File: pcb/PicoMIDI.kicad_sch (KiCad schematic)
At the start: 11 parts, among them J1 DIN-5, J2 DIN-5, J3 AudioJack3_SwitchTR, J4 AudioJack3_SwitchTR, U1 RP2040, U2 6N138

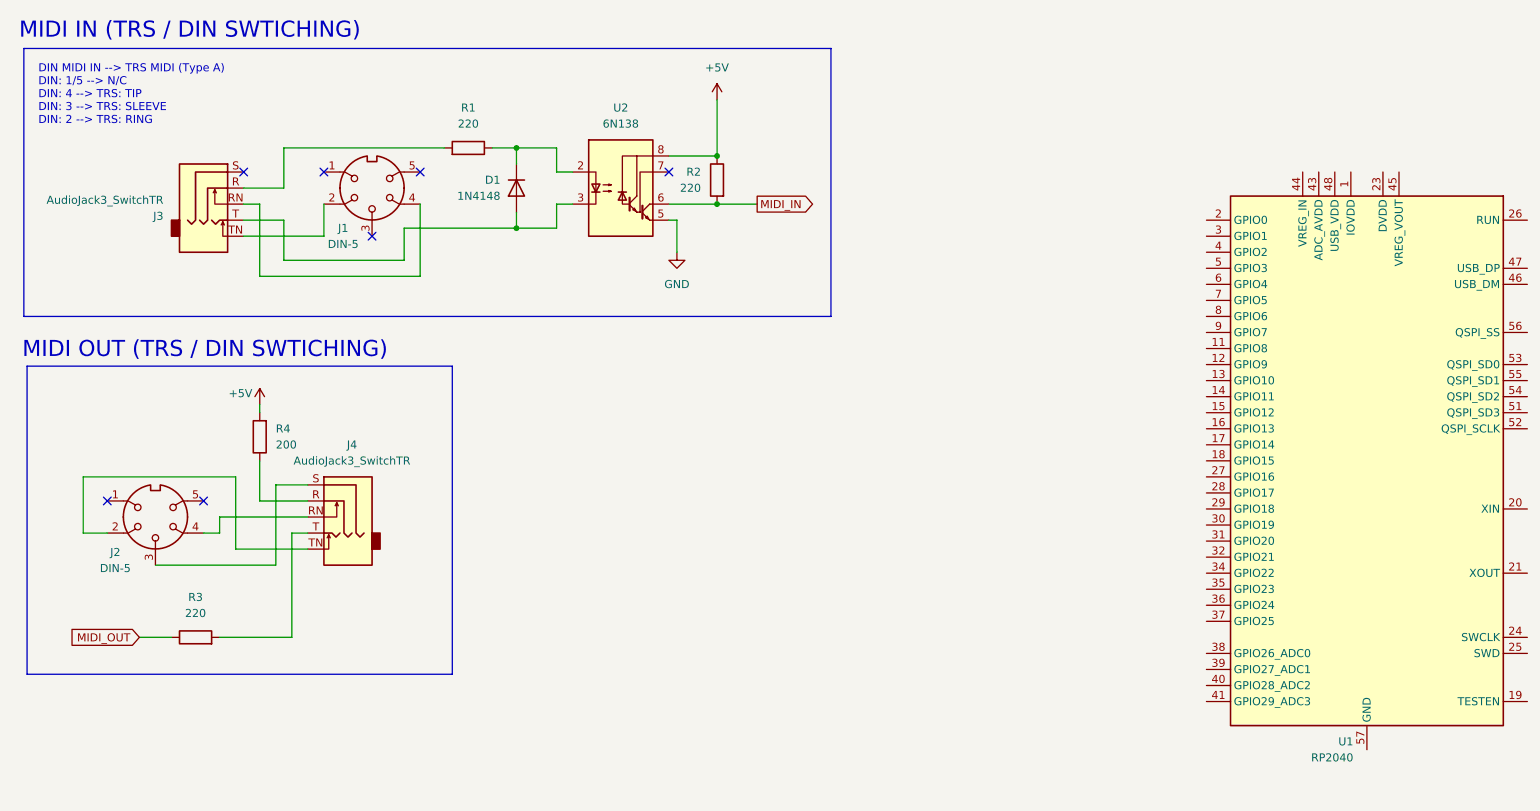
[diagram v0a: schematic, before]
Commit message: update schematic
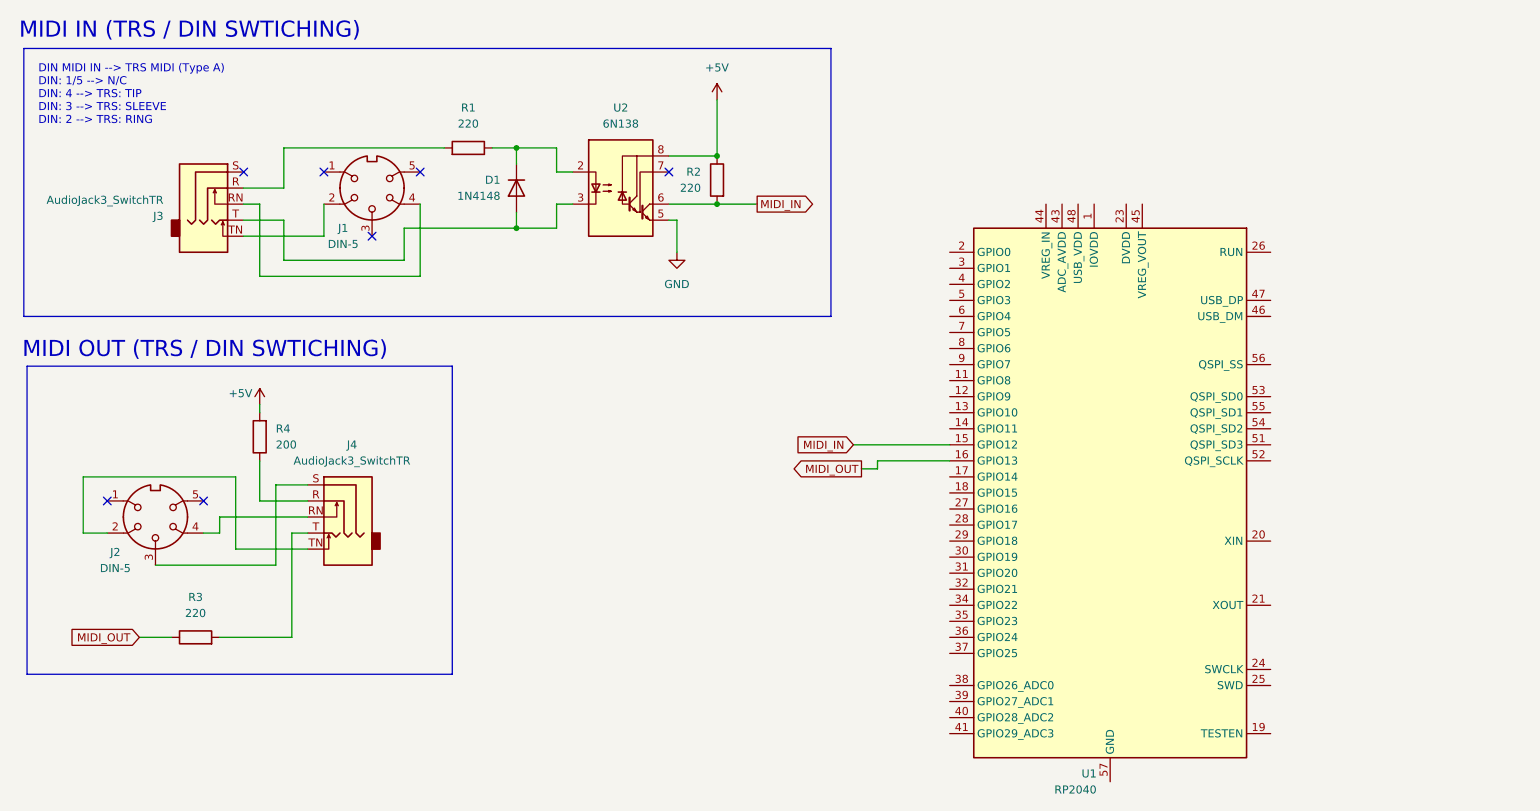
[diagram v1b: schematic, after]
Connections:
- net MIDI_IN: now also U1.15 (GPIO12)
- net MIDI_OUT: now also U1.16 (GPIO13)
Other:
- moved on the sheet: U1
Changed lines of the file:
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@@
+	(wire
+		(pts
+			(xy 149.86 86.36) (xy 161.29 86.36)
+		)
+		(stroke
+			(width 0)
+			(type default)
+		)
+	)
 	(wire
 		(pts
@@
 	(wire
 		(pts
+			(xy 146.05 83.82) (xy 161.29 83.82)
+		)
+		(stroke
+			(width 0)
+			(type default)
+		)
+	)
+	(wire
+		(pts
 			(xy 55.88 54.61) (xy 55.88 48.26)
 		)
@@
 	(wire
 		(pts
+			(xy 147.32 87.63) (xy 149.86 87.63)
+		)
+		(stroke
+			(width 0)
+			(type default)
+		)
+	)
+	(wire
+		(pts
 			(xy 54.61 90.17) (xy 59.69 90.17)
 		)
@@
 			(type default)
 			(color 132 0 132 1)
+		)
+	)
+	(wire
+		(pts
+			(xy 149.86 87.63) (xy 149.86 86.36)
+		)
+		(stroke
+			(width 0)
+			(type default)
 		)
 	)
@@
 	)
 	(global_label "MIDI_IN"
+		(shape input)
+		(at 146.05 83.82 180)
+		(fields_autoplaced yes)
+		(effects
+			(font
+				(size 1.27 1.27)
+			)
+			(justify right)
+		)
+		(property "Intersheetrefs" "${INTERSHEET_REFS}"
+			(at 136.2309 83.82 0)
+			(effects
+				(font
+					(size 1.27 1.27)
+				)
+				(justify right)
+				(hide yes)
+			)
+		)
+	)
+	(global_label "MIDI_IN"
 		(shape output)
 		(at 130.81 45.72 0)
@@
 				)
 				(justify left)
+				(hide yes)
+			)
+		)
+	)
+	(global_label "MIDI_OUT"
+		(shape output)
+		(at 147.32 87.63 180)
+		(fields_autoplaced yes)
+		(effects
+			(font
+				(size 1.27 1.27)
+			)
+			(justify right)
+		)
+		(property "Intersheetrefs" "${INTERSHEET_REFS}"
+			(at 135.8076 87.63 0)
+			(effects
+				(font
+					(size 1.27 1.27)
+				)
+				(justify right)
 				(hide yes)
 			)
@@
 	(symbol
 		(lib_id "MCU_RaspberryPi:RP2040")
-		(at 227.33 86.36 0)
+		(at 186.69 91.44 0)
 		(mirror y)
 		(unit 1)
@@
 		(dnp no)
 		(property "Reference" "U1"
-			(at 225.1867 130.81 0)
+			(at 184.5467 135.89 0)
 			(effects
 				(font
@@
 		)
 		(property "Value" "RP2040"
-			(at 225.1867 133.35 0)
+			(at 184.5467 138.43 0)
 			(effects
 				(font
@@
 		)
 		(property "Footprint" "Package_DFN_QFN:QFN-56-1EP_7x7mm_P0.4mm_EP3.2x3.2mm"
-			(at 227.33 86.36 0)
+			(at 186.69 91.44 0)
 			(effects
 				(font
@@
 		)
 		(property "Datasheet" "https://datasheets.raspberrypi.com/rp2040/rp2040-datasheet.pdf"
-			(at 227.33 86.36 0)
+			(at 186.69 91.44 0)
 			(effects
 				(font
@@
 		)
 		(property "Description" "A microcontroller by Raspberry Pi"
-			(at 227.33 86.36 0)
-			(effects
-				(font
+			(at 186.69 91.44 0)
+			(effects
+				(font
